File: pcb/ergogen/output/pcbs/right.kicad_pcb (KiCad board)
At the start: 2 copper layers, 136.9 x 74.7 mm, 49 parts

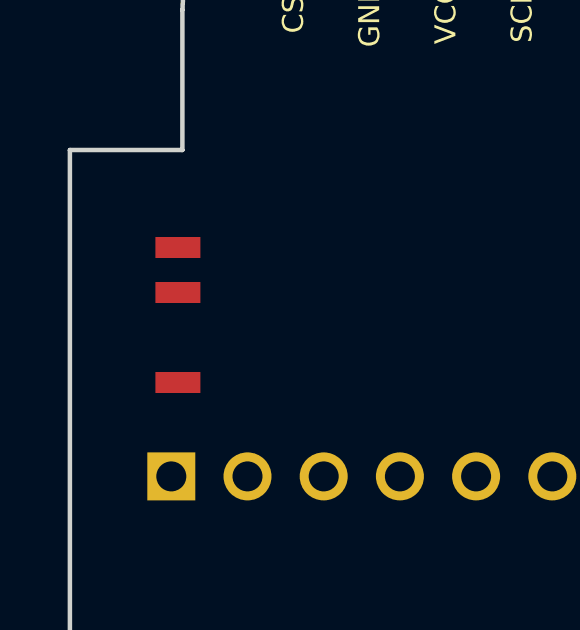
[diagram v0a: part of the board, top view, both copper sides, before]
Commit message: Power switch placeholder: match SW_SPDT_PCM12 pad layout and orientation
The placeholder had its pads on the opposite side to KiCad's PCM12, so
'Change Footprint' left the lever pointing into the board. Pads now
match PCM12 (pins at -y, lever at +y) and the rotations point the lever
out through the side wall on both halves.

Co-Authored-By: Claude Opus 5.5 <noreply@anthropic.com>
Claude-Session: https://claude.ai/code/session_017zNm7dMSTHELcztuNr6aNy
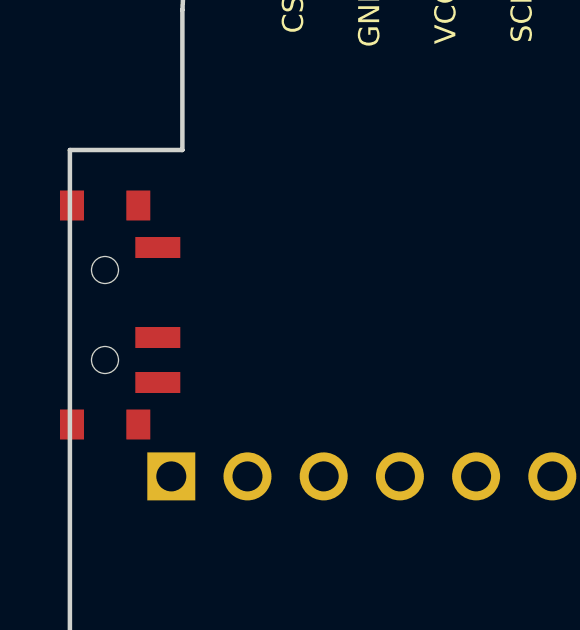
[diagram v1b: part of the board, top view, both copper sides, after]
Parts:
- turned PWR1 to -90 degrees
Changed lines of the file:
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@@
       )
     (module kataware_power_switch_placeholder (layer F.Cu)
-    (at 188.97500000000002 -51.50000000000001 90)
-    (fp_text reference "PWR1" (at 0 -3) (layer F.SilkS) hide (effects (font (size 1 1) (thickness 0.15))))
+    (at 188.97500000000002 -51.50000000000001 -90)
+    (fp_text reference "PWR1" (at 0 -3.2 -90) (layer F.SilkS) hide (effects (font (size 1 1) (thickness 0.15))))
     (fp_text value "" (at 0 0) (layer F.SilkS) hide (effects (font (size 1 1) (thickness 0.15))))
-    (fp_text user "PWR (仮)" (at 0 3 90) (layer F.Fab) (effects (font (size 0.8 0.8) (thickness 0.12))))
-    (fp_line (start -3.35 -1.4) (end 3.35 -1.4) (layer F.Fab) (width 0.12))
-    (fp_line (start 3.35 -1.4) (end 3.35 1.4) (layer F.Fab) (width 0.12))
-    (fp_line (start 3.35 1.4) (end -3.35 1.4) (layer F.Fab) (width 0.12))
-    (fp_line (start -3.35 1.4) (end -3.35 -1.4) (layer F.Fab) (width 0.12))
-    (pad 1 smd rect (at -2.25 2.1 90) (size 0.7 1.5) (layers F.Cu F.Paste F.Mask) (net 43 "BAT_P"))
-    (pad 2 smd rect (at 0.75 2.1 90) (size 0.7 1.5) (layers F.Cu F.Paste F.Mask) (net 42 "BAT_SW"))
-    (pad 3 smd rect (at 2.25 2.1 90) (size 0.7 1.5) (layers F.Cu F.Paste F.Mask))
+    (fp_text user "PWR (仮)" (at 0 0.3 -90) (layer F.Fab) (effects (font (size 0.6 0.6) (thickness 0.1))))
+    (fp_line (start -3.35 -1) (end 3.35 -1) (layer F.Fab) (width 0.1))
+    (fp_line (start 3.35 -1) (end 3.35 1.6) (layer F.Fab) (width 0.1))
+    (fp_line (start 3.35 1.6) (end -3.35 1.6) (layer F.Fab) (width 0.1))
+    (fp_line (start -3.35 1.6) (end -3.35 -1) (layer F.Fab) (width 0.1))
+    (fp_line (start -1.4 1.6) (end -1.4 3.15) (layer F.Fab) (width 0.1))
+    (fp_line (start -1.4 3.15) (end -0.1 3.15) (layer F.Fab) (width 0.1))
+    (fp_line (start -0.1 3.15) (end -0.1 1.6) (layer F.Fab) (width 0.1))
+    (fp_text user "レバー" (at -0.75 4.2 -90) (layer F.Fab) (effects (font (size 0.5 0.5) (thickness 0.08))))
+    (pad 1 smd rect (at -2.25 -1.43 -90) (size 0.7 1.5) (layers F.Cu F.Paste F.Mask) (net 43 "BAT_P"))
+    (pad 2 smd rect (at 0.75 -1.43 -90) (size 0.7 1.5) (layers F.Cu F.Paste F.Mask) (net 42 "BAT_SW"))
+    (pad 3 smd rect (at 2.25 -1.43 -90) (size 0.7 1.5) (layers F.Cu F.Paste F.Mask))
+    (pad "" smd rect (at -3.65 -0.78 -90) (size 1 0.8) (layers F.Cu F.Paste F.Mask))
+    (pad "" smd rect (at -3.65 1.43 -90) (size 1 0.8) (layers F.Cu F.Paste F.Mask))
+    (pad "" smd rect (at 3.65 -0.78 -90) (size 1 0.8) (layers F.Cu F.Paste F.Mask))
+    (pad "" smd rect (at 3.65 1.43 -90) (size 1 0.8) (layers F.Cu F.Paste F.Mask))
+    (pad "" np_thru_hole circle (at -1.5 0.33) (size 0.9 0.9) (drill 0.9) (layers *.Cu *.Mask))
+    (pad "" np_thru_hole circle (at 1.5 0.33) (size 0.9 0.9) (drill 0.9) (layers *.Cu *.Mask))
     )
     (module kataware_battery_125_placeholder (layer B.Cu)

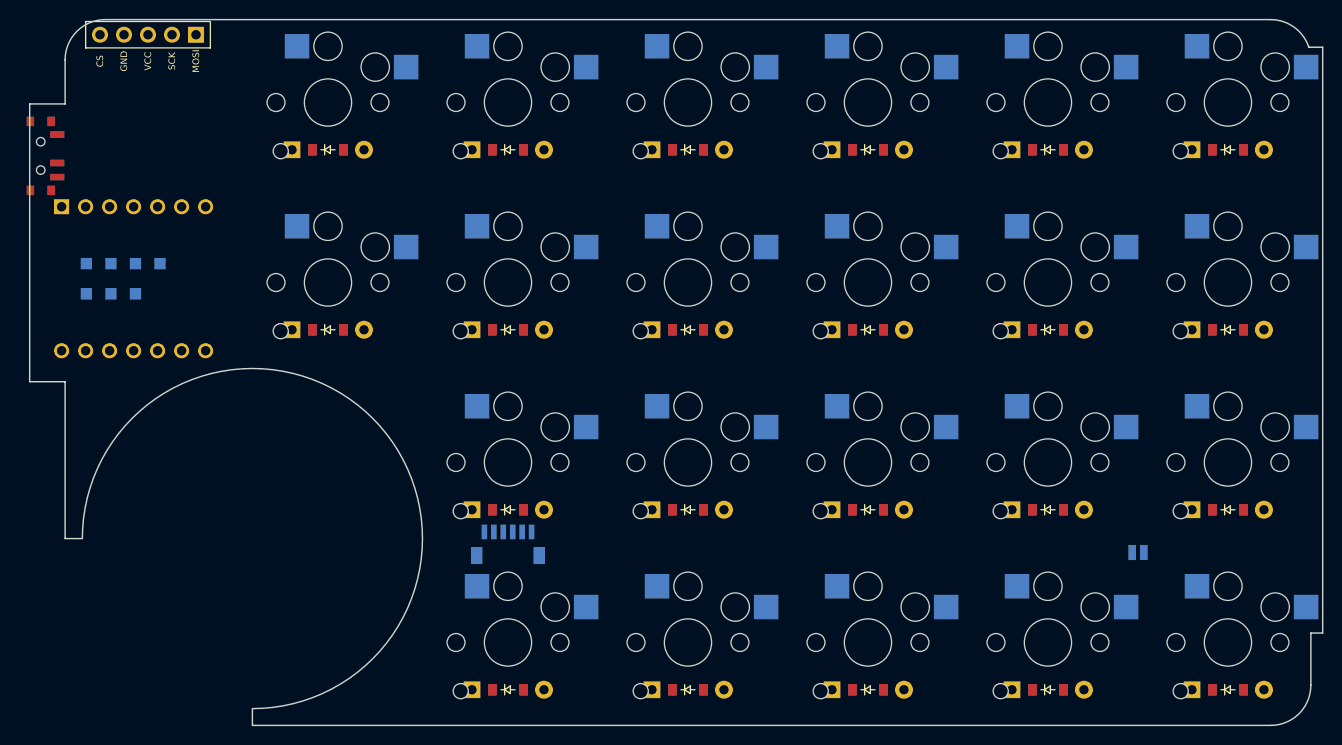
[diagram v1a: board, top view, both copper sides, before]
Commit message: Use real footprints for XIAO Plus, power switch and connectors
- tools/import_footprints.py converts .kicad_mod files (vendored in
  pcb/ergogen/lib_src) into Ergogen footprints with per-pad nets and
  back-side mirroring; KiCad library PCM12, JST SH BM06B and Molex
  PicoBlade, plus Seeed's official XIAO nRF52840 Plus (CC-BY-SA, credited)
- XIAO pad 28 (VBAT) gets a 0.7mm through-hole so it can be soldered
  from the front, as it sits hidden under the module
- Power switch moved 0.65mm inwards so its mounting pads stay on the
  board; battery connectors rotated to face the battery
- Diodes moved 2mm right: their THT pad overlapped the switch's 1.6mm
  locating hole on every key
- tools/check_pcb.py: pad clearance and board-edge check (clean)
- Placeholders removed; README and KiCad guide updated

Co-Authored-By: Claude Opus 5.5 <noreply@anthropic.com>
Claude-Session: https://claude.ai/code/session_017zNm7dMSTHELcztuNr6aNy
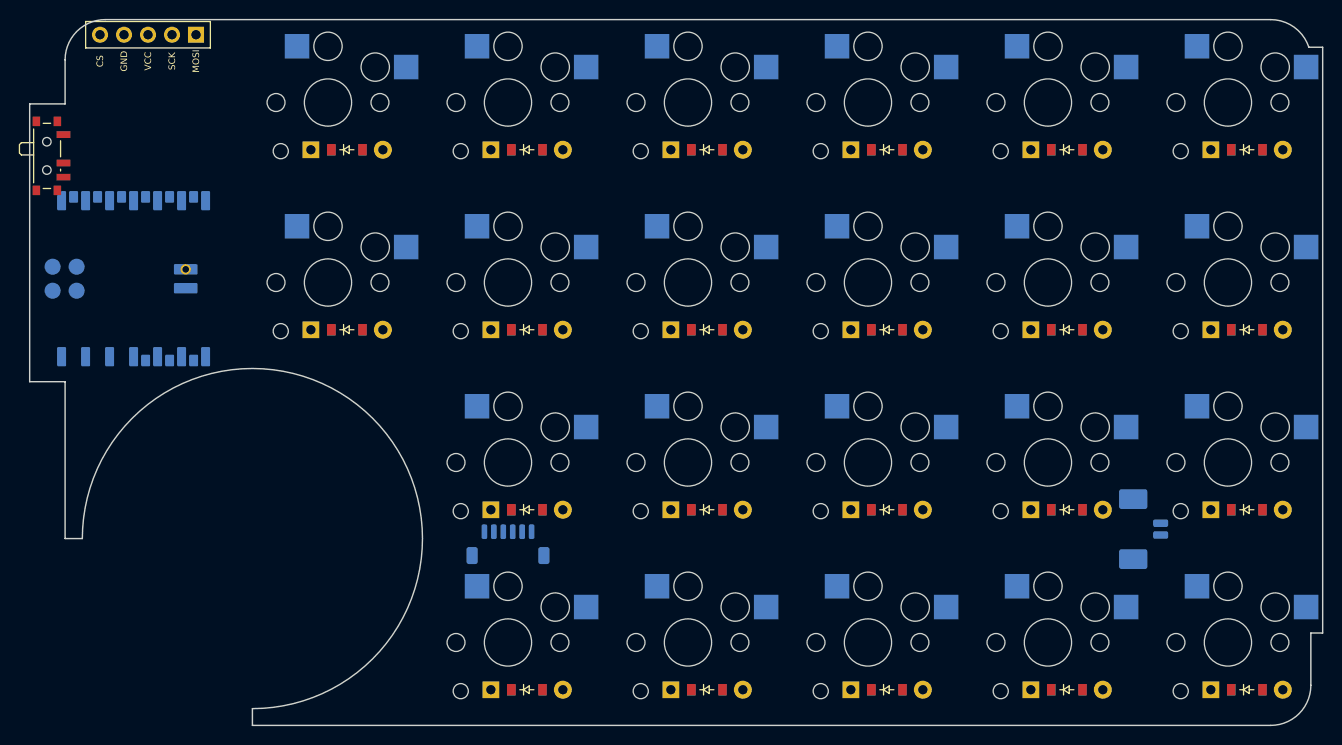
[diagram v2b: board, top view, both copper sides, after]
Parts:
- BAT1: value (none) -> Molex_PicoBlade_53261-0271_1x02-1MP_P1.25mm_Horizontal; footprint kataware_battery_125_placeholder -> Connector_Molex:Molex_PicoBlade_53261-0271_1x02-1MP_P1.25mm_Horizontal
- J1: value (none) -> JST_SH_BM06B-SRSS-TB_1x06-1MP_P1.00mm_Vertical; footprint kataware_jst_sh6_placeholder -> Connector_JST:JST_SH_BM06B-SRSS-TB_1x06-1MP_P1.00mm_Vertical
- MCU1: value (none) -> XIAO-nRF52840-Plus-SMD; footprint kataware_xiao_plus_placeholder -> Seeed_Studio_XIAO_Series:XIAO-nRF52840-Plus-SMD
- PWR1: value (none) -> SW_SPDT_PCM12; footprint kataware_power_switch_placeholder -> Button_Switch_SMD:SW_SPDT_PCM12
- moved BAT1 2.47 mm to (304.8, -12.0), turned to 90 degrees
- moved D1 2.00 mm to (221.1, -33.1)
- moved D10 2.00 mm to (259.2, -52.2)
- moved D11 2.00 mm to (278.2, 5.00)
- moved D12 2.00 mm to (278.2, -14.1)
- moved D13 2.00 mm to (278.2, -33.1)
- moved D14 2.00 mm to (278.2, -52.2)
- moved D15 2.00 mm to (297.2, 5.00)
- moved D16 2.00 mm to (297.2, -14.1)
- moved D17 2.00 mm to (297.2, -33.1)
- moved D18 2.00 mm to (297.2, -52.2)
- moved D19 2.00 mm to (316.3, 5.00)
- moved D2 2.00 mm to (221.1, -52.2)
- moved D20 2.00 mm to (316.3, -14.1)
- moved D21 2.00 mm to (316.3, -33.1)
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
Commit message: Ukishima: production data (tray, ball units, PCB nuts, plates)
- case/ukishima.py builds printable STLs into case/stl/ukishima/ and checks fit
- PCB: M2 SMT nuts at the 8 post positions; battery connectors moved beside
  the relocated batteries; encoder diode shifted off a post
- Plates lose the gasket tabs; nice!view corner cut so no thin slivers remain
- check_pcb.py also checks back-side part overlap and parts above the battery
- docs/ukishima-build.md: BOM, printing and assembly; gasket case kept as old version

Co-Authored-By: Claude Opus 5.5 <noreply@anthropic.com>
Claude-Session: https://claude.ai/code/session_017zNm7dMSTHELcztuNr6aNy
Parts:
- added H1: SMT_Nut_M2, kataware:SMT_Nut_M2, B.Cu at (247.6, -9.53)
- added H2: SMT_Nut_M2, kataware:SMT_Nut_M2, B.Cu at (285.7, -9.53)
- added H3: SMT_Nut_M2, kataware:SMT_Nut_M2, B.Cu at (228.6, -28.6)
- added H4: SMT_Nut_M2, kataware:SMT_Nut_M2, B.Cu at (228.6, -47.6)
- added H5: SMT_Nut_M2, kataware:SMT_Nut_M2, B.Cu at (266.7, -47.6)
- added H6: SMT_Nut_M2, kataware:SMT_Nut_M2, B.Cu at (304.8, -47.6)
- added H7: SMT_Nut_M2, kataware:SMT_Nut_M2, B.Cu at (266.7, -28.6)
- added H8: SMT_Nut_M2, kataware:SMT_Nut_M2, B.Cu at (304.8, -28.6)
- moved BAT1 25.3 mm to (286.0, -29.0), turned to -90 degrees
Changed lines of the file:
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@@
   (title_block
     (title "right")
-    (date "2026-10-18")
+    (date "2026-10-19")
     (rev "0.1")
     (company "kyonccc")
@@
       (model "${KICAD10_3DMODEL_DIR}/Button_Switch_SMD.3dshapes/SW_SPDT_PCM12.step")
       )
+      (module "kataware:SMT_Nut_M2" (layer B.Cu)
+      (at 247.625 -9.525000000000006 0)
+      (fp_text reference "H1" (at 0 3.6 0) (layer B.SilkS) hide (effects (font (size 0.8 0.8) (thickness 0.12)) (justify mirror)))
+      (fp_text value "SMT_Nut_M2" (at 0 0 0) (layer B.Fab) hide (effects (font (size 0.8 0.8) (thickness 0.12))))
+      (fp_circle (center 0 0) (end 1.9 0) (layer B.Fab) (width 0.1))
+      (fp_circle (center 0 0) (end 2.75 0) (layer B.CrtYd) (width 0.05))
+      (fp_circle (center 0 0) (end 2.7 0) (layer B.SilkS) (width 0.12))
+      (pad "" thru_hole circle (at 0 0 0) (size 5.0 5.0) (drill 2.4) (layers *.Cu B.Mask B.Paste))
+      )
+      (module "kataware:SMT_Nut_M2" (layer B.Cu)
+      (at 285.725 -9.525000000000006 0)
+      (fp_text reference "H2" (at 0 3.6 0) (layer B.SilkS) hide (effects (font (size 0.8 0.8) (thickness 0.12)) (justify mirror)))
+      (fp_text value "SMT_Nut_M2" (at 0 0 0) (layer B.Fab) hide (effects (font (size 0.8 0.8) (thickness 0.12))))
+      (fp_circle (center 0 0) (end 1.9 0) (layer B.Fab) (width 0.1))
+      (fp_circle (center 0 0) (end 2.75 0) (layer B.CrtYd) (width 0.05))
+      (fp_circle (center 0 0) (end 2.7 0) (layer B.SilkS) (width 0.12))
+      (pad "" thru_hole circle (at 0 0 0) (size 5.0 5.0) (drill 2.4) (layers *.Cu B.Mask B.Paste))
+      )
+      (module "kataware:SMT_Nut_M2" (layer B.Cu)
+      (at 228.57500000000002 -28.575000000000006 0)
+      (fp_text reference "H3" (at 0 3.6 0) (layer B.SilkS) hide (effects (font (size 0.8 0.8) (thickness 0.12)) (justify mirror)))
+      (fp_text value "SMT_Nut_M2" (at 0 0 0) (layer B.Fab) hide (effects (font (size 0.8 0.8) (thickness 0.12))))
+      (fp_circle (center 0 0) (end 1.9 0) (layer B.Fab) (width 0.1))
+      (fp_circle (center 0 0) (end 2.75 0) (layer B.CrtYd) (width 0.05))
+      (fp_circle (center 0 0) (end 2.7 0) (layer B.SilkS) (width 0.12))
+      (pad "" thru_hole circle (at 0 0 0) (size 5.0 5.0) (drill 2.4) (layers *.Cu B.Mask B.Paste))
+      )
+      (module "kataware:SMT_Nut_M2" (layer B.Cu)
+      (at 228.57500000000002 -47.62500000000001 0)
+      (fp_text reference "H4" (at 0 3.6 0) (layer B.SilkS) hide (effects (font (size 0.8 0.8) (thickness 0.12)) (justify mirror)))
+      (fp_text value "SMT_Nut_M2" (at 0 0 0) (layer B.Fab) hide (effects (font (size 0.8 0.8) (thickness 0.12))))
+      (fp_circle (center 0 0) (end 1.9 0) (layer B.Fab) (width 0.1))
+      (fp_circle (center 0 0) (end 2.75 0) (layer B.CrtYd) (width 0.05))
+      (fp_circle (center 0 0) (end 2.7 0) (layer B.SilkS) (width 0.12))
+      (pad "" thru_hole circle (at 0 0 0) (size 5.0 5.0) (drill 2.4) (layers *.Cu B.Mask B.Paste))
+      )
+      (module "kataware:SMT_Nut_M2" (layer B.Cu)
+      (at 266.675 -47.62500000000001 0)
+      (fp_text reference "H5" (at 0 3.6 0) (layer B.SilkS) hide (effects (font (size 0.8 0.8) (thickness 0.12)) (justify mirror)))
+      (fp_text value "SMT_Nut_M2" (at 0 0 0) (layer B.Fab) hide (effects (font (size 0.8 0.8) (thickness 0.12))))
+      (fp_circle (center 0 0) (end 1.9 0) (layer B.Fab) (width 0.1))
+      (fp_circle (center 0 0) (end 2.75 0) (layer B.CrtYd) (width 0.05))
+      (fp_circle (center 0 0) (end 2.7 0) (layer B.SilkS) (width 0.12))
+      (pad "" thru_hole circle (at 0 0 0) (size 5.0 5.0) (drill 2.4) (layers *.Cu B.Mask B.Paste))
+      )
+      (module "kataware:SMT_Nut_M2" (layer B.Cu)
+      (at 304.775 -47.62500000000001 0)
+      (fp_text reference "H6" (at 0 3.6 0) (layer B.SilkS) hide (effects (font (size 0.8 0.8) (thickness 0.12)) (justify mirror)))
+      (fp_text value "SMT_Nut_M2" (at 0 0 0) (layer B.Fab) hide (effects (font (size 0.8 0.8) (thickness 0.12))))
+      (fp_circle (center 0 0) (end 1.9 0) (layer B.Fab) (width 0.1))
+      (fp_circle (center 0 0) (end 2.75 0) (layer B.CrtYd) (width 0.05))
+      (fp_circle (center 0 0) (end 2.7 0) (layer B.SilkS) (width 0.12))
+      (pad "" thru_hole circle (at 0 0 0) (size 5.0 5.0) (drill 2.4) (layers *.Cu B.Mask B.Paste))
+      )
+      (module "kataware:SMT_Nut_M2" (layer B.Cu)
+      (at 266.675 -28.575000000000006 0)
+      (fp_text reference "H7" (at 0 3.6 0) (layer B.SilkS) hide (effects (font (size 0.8 0.8) (thickness 0.12)) (justify mirror)))
+      (fp_text value "SMT_Nut_M2" (at 0 0 0) (layer B.Fab) hide (effects (font (size 0.8 0.8) (thickness 0.12))))
+      (fp_circle (center 0 0) (end 1.9 0) (layer B.Fab) (width 0.1))
+      (fp_circle (center 0 0) (end 2.75 0) (layer B.CrtYd) (width 0.05))
+      (fp_circle (center 0 0) (end 2.7 0) (layer B.SilkS) (width 0.12))
+      (pad "" thru_hole circle (at 0 0 0) (size 5.0 5.0) (drill 2.4) (layers *.Cu B.Mask B.Paste))
+      )
+      (module "kataware:SMT_Nut_M2" (layer B.Cu)
+      (at 304.775 -28.575000000000006 0)
+      (fp_text reference "H8" (at 0 3.6 0) (layer B.SilkS) hide (effects (font (size 0.8 0.8) (thickness 0.12)) (justify mirror)))
+      (fp_text value "SMT_Nut_M2" (at 0 0 0) (layer B.Fab) hide (effects (font (size 0.8 0.8) (thickness 0.12))))
+      (fp_circle (center 0 0) (end 1.9 0) (layer B.Fab) (width 0.1))
+      (fp_circle (center 0 0) (end 2.75 0) (layer B.CrtYd) (width 0.05))
+      (fp_circle (center 0 0) (end 2.7 0) (layer B.SilkS) (width 0.12))
+      (pad "" thru_hole circle (at 0 0 0) (size 5.0 5.0) (drill 2.4) (layers *.Cu B.Mask B.Paste))
+      )
       (module "Connector_Molex:Molex_PicoBlade_53261-0271_1x02-1MP_P1.25mm_Horizontal" (layer B.Cu)
-      (at 304.77500000000003 -12 90)
-      (fp_text reference "BAT1" (at 0 4.4 90) (layer B.SilkS) hide (effects (font (size 1 1) (thickness 0.15)) (justify mirror)))
-      (fp_text value "Molex_PicoBlade_53261-0271_1x02-1MP_P1.25mm_Horizontal" (at 0 0 90) (layer B.Fab) hide (effects (font (size 0.8 0.8) (thickness 0.12)) (justify mirror)))
+      (at 286 -29 -90)
+      (fp_text reference "BAT1" (at 0 4.4 -90) (layer B.SilkS) hide (effects (font (size 1 1) (thickness 0.15)) (justify mirror)))
+      (fp_text value "Molex_PicoBlade_53261-0271_1x02-1MP_P1.25mm_Horizontal" (at 0 0 -90) (layer B.Fab) hide (effects (font (size 0.8 0.8) (thickness 0.12)) (justify mirror)))
       (fp_line (start -2.235 1.71) (end -1.285 1.71) (layer B.SilkS) (width 0.12))
       (fp_line (start -2.235 1.26) (end -2.235 1.71) (layer B.SilkS) (width 0.12))
@@
       (fp_line (start 3.825 0.4) (end 3.825 -1.4) (layer B.Fab) (width 0.1))
       (fp_line (start 3.825 -1.4) (end 3.625 -1.6) (layer B.Fab) (width 0.1))
-      (pad "1" smd roundrect (at -0.625 2.4 90) (size 0.8 1.6) (roundrect_rratio 0.25) (layers B.Cu B.Mask B.Paste) (net 34 "GND"))
-      (pad "2" smd roundrect (at 0.625 2.4 90) (size 0.8 1.6) (roundrect_rratio 0.25) (layers B.Cu B.Mask B.Paste) (net 43 "BAT_P"))
-      (pad "MP" smd roundrect (at -3.175 -0.5 90) (size 2.1 3) (roundrect_rratio 0.119048) (layers B.Cu B.Mask B.Paste))
-      (pad "MP" smd roundrect (at 3.175 -0.5 90) (size 2.1 3) (roundrect_rratio 0.119048) (layers B.Cu B.Mask B.Paste))
+      (pad "1" smd roundrect (at -0.625 2.4 -90) (size 0.8 1.6) (roundrect_rratio 0.25) (layers B.Cu B.Mask B.Paste) (net 34 "GND"))
+      (pad "2" smd roundrect (at 0.625 2.4 -90) (size 0.8 1.6) (roundrect_rratio 0.25) (layers B.Cu B.Mask B.Paste) (net 43 "BAT_P"))
+      (pad "MP" smd roundrect (at -3.175 -0.5 -90) (size 2.1 3) (roundrect_rratio 0.119048) (layers B.Cu B.Mask B.Paste))
+      (pad "MP" smd roundrect (at 3.175 -0.5 -90) (size 2.1 3) (roundrect_rratio 0.119048) (layers B.Cu B.Mask B.Paste))
       (model "${KICAD10_3DMODEL_DIR}/Connector_Molex.3dshapes/Molex_PicoBlade_53261-0271_1x02-1MP_P1.25mm_Horizontal.step")
       )
